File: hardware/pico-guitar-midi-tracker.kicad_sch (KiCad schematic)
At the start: 22 parts, among them J1 Barrel_Jack_Switch, J2 AudioJack3_Switch, J4 MIDIOUT, J5 MIDIOUT, U2 LM386, U3 Pico, U4 L7805

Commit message: Updated capacitor values.
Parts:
- removed C2, C3: C, symbol Device:C
- added C2, C9: 22uF, symbol Device:C_Polarized
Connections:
- net +5V: now also C2.1
- net +9V: now also C9.1
- net GND: now also C2.2, C9.2
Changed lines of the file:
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@@
+    )
+  )
+  (symbol (lib_id "Device:C_Polarized") (at 104.14 142.24 0) (unit 1)
+    (in_bom yes) (on_board yes) (dnp no) (fields_autoplaced)
+    (property "Reference" "C2" (at 107.95 140.081 0)
+      (effects (font (size 1.27 1.27)) (justify left))
+    )
+    (property "Value" "22uF" (at 107.95 142.621 0)
+      (effects (font (size 1.27 1.27)) (justify left))
+    )
+    (property "Footprint" "" (at 105.1052 146.05 0)
+      (effects (font (size 1.27 1.27)) hide)
+    )
+    (property "Datasheet" "~" (at 104.14 142.24 0)
+      (effects (font (size 1.27 1.27)) hide)
+    )
+    (pin "1")
+    (pin "2")
+    (instances
+      (project "pico-guitar-midi-tracker"
+        (path "/5d23c65d-b53e-49fe-b7b6-37427454671d"
+          (reference "C2") (unit 1)
+        )
+      )
     )
   )
@@
         (path "/5d23c65d-b53e-49fe-b7b6-37427454671d"
           (reference "#PWR02") (unit 1)
-        )
-      )
-    )
-  )
-  (symbol (lib_id "Device:C") (at 104.14 142.24 0) (unit 1)
-    (in_bom yes) (on_board yes) (dnp no) (fields_autoplaced)
-    (property "Reference" "C3" (at 107.95 140.97 0)
-      (effects (font (size 1.27 1.27)) (justify left))
-    )
-    (property "Value" "C" (at 107.95 143.51 0)
-      (effects (font (size 1.27 1.27)) (justify left))
-    )
-    (property "Footprint" "" (at 105.1052 146.05 0)
-      (effects (font (size 1.27 1.27)) hide)
-    )
-    (property "Datasheet" "~" (at 104.14 142.24 0)
-      (effects (font (size 1.27 1.27)) hide)
-    )
-    (pin "1")
-    (pin "2")
-    (instances
-      (project "pico-guitar-midi-tracker"
-        (path "/5d23c65d-b53e-49fe-b7b6-37427454671d"
-          (reference "C3") (unit 1)
         )
       )
@@
     )
   )
+  (symbol (lib_id "Device:C_Polarized") (at 74.93 142.24 0) (unit 1)
+    (in_bom yes) (on_board yes) (dnp no) (fields_autoplaced)
+    (property "Reference" "C9" (at 78.74 140.081 0)
+      (effects (font (size 1.27 1.27)) (justify left))
+    )
+    (property "Value" "22uF" (at 78.74 142.621 0)
+      (effects (font (size 1.27 1.27)) (justify left))
+    )
+    (property "Footprint" "" (at 75.8952 146.05 0)
+      (effects (font (size 1.27 1.27)) hide)
+    )
+    (property "Datasheet" "~" (at 74.93 142.24 0)
+      (effects (font (size 1.27 1.27)) hide)
+    )
+    (pin "1")
+    (pin "2")
+    (instances
+      (project "pico-guitar-midi-tracker"
+        (path "/5d23c65d-b53e-49fe-b7b6-37427454671d"
+          (reference "C9") (unit 1)
+        )
+      )
+    )
+  )
   (symbol (lib_id "power:GND") (at 168.91 143.51 0) (unit 1)
     (in_bom yes) (on_board yes) (dnp no) (fields_autoplaced)
@@
         )
       )
-    )
-  )
-  (symbol (lib_id "Device:C") (at 74.93 142.24 0) (unit 1)
-    (in_bom yes) (on_board yes) (dnp no) (fields_autoplaced)
-    (property "Reference" "C2" (at 78.74 140.97 0)
-      (effects (font (size 1.27 1.27)) (justify left))
-    )
-    (property "Value" "C" (at 78.74 143.51 0)
-      (effects (font (size 1.27 1.27)) (justify left))
-    )
-    (property "Footprint" "" (at 75.8952 146.05 0)
-      (effects (font (size 1.27 1.27)) hide)
-    )
-    (property "Datasheet" "~" (at 74.93 142.24 0)
-      (effects (font (size 1.27 1.27)) hide)
-    )
-    (pin "1")
-    (pin "2")
-    (instances
-      (project "pico-guitar-midi-tracker"
-        (path "/5d23c65d-b53e-49fe-b7b6-37427454671d"
-          (reference "C2") (unit 1)
-        )
-      )

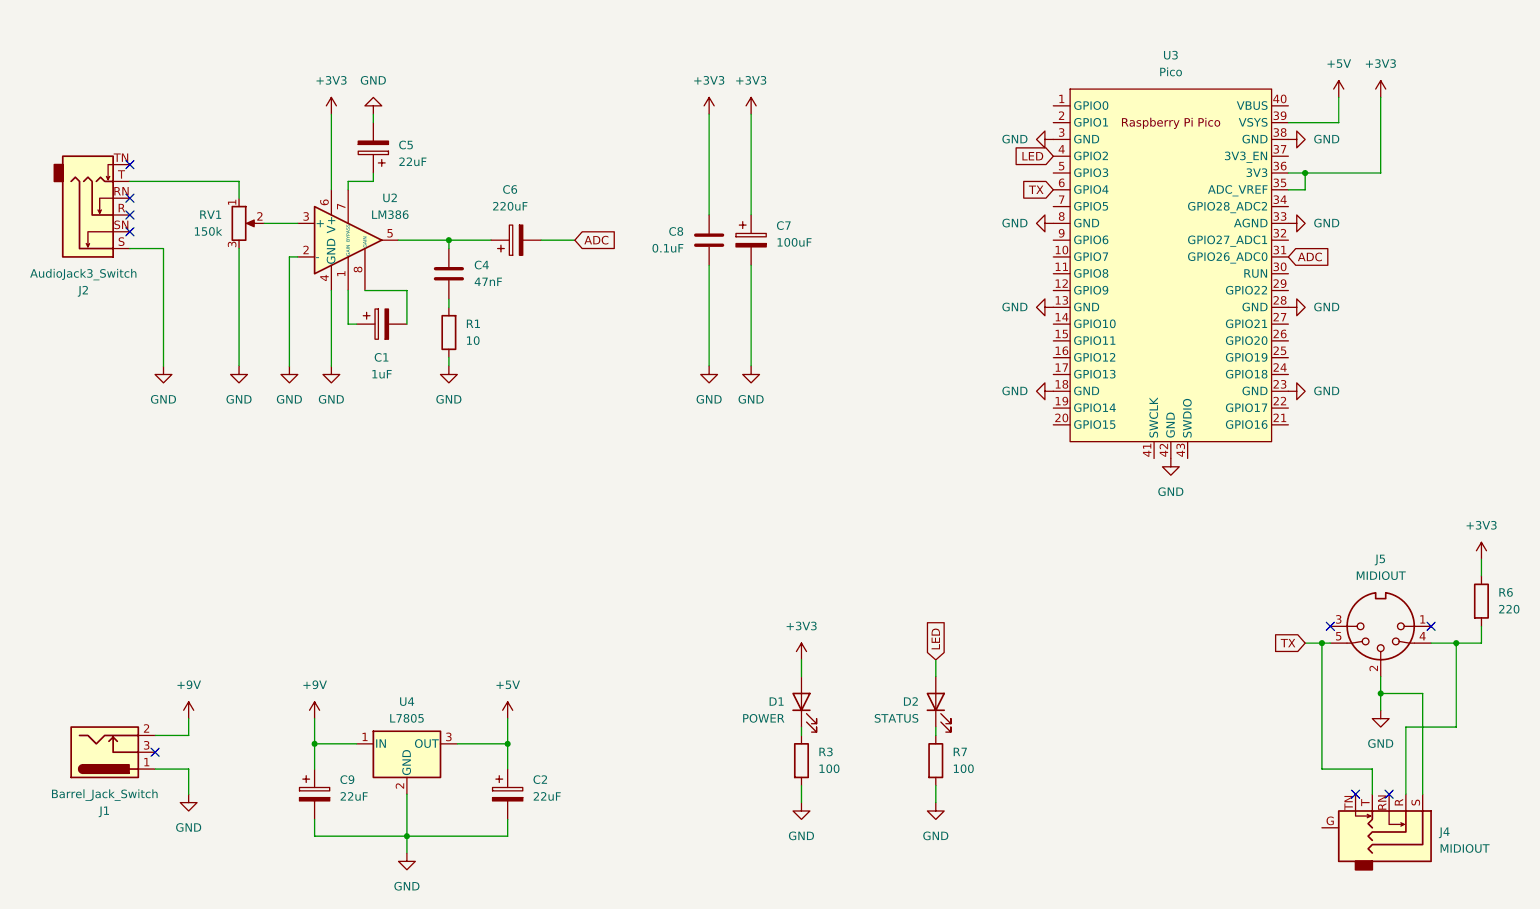
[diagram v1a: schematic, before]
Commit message: Added schematic info and pdf.
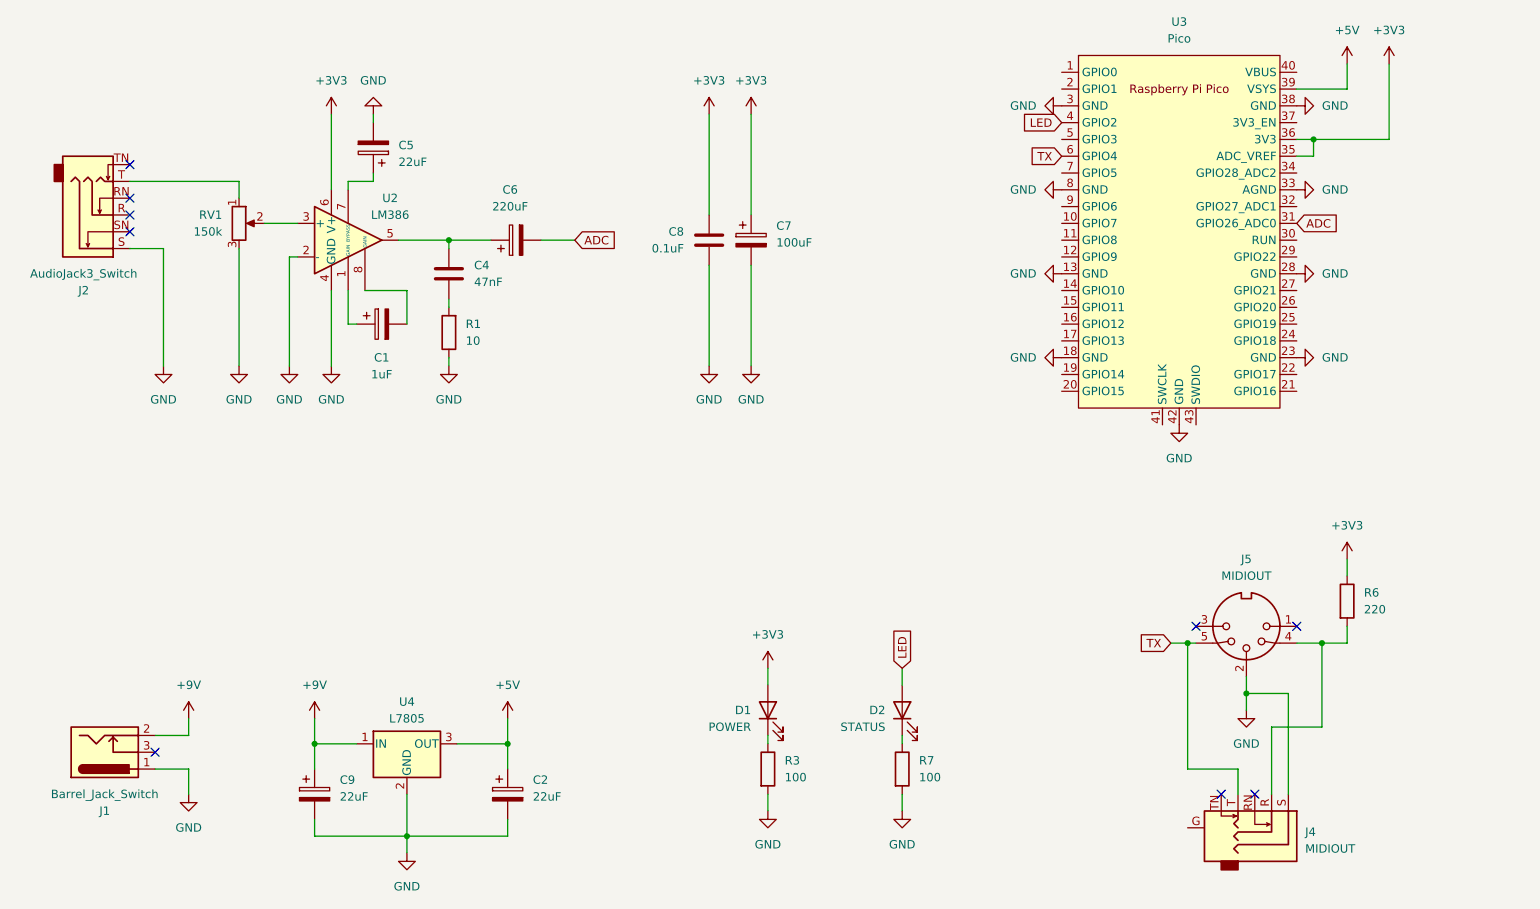
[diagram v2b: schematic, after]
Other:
- company: (none) -> D Cooper Dalrymple
- title: (none) -> Pico Guitar Midi Tracker
- moved on the sheet: D1, D2, J4, J5, R3, R6, R7, U3
